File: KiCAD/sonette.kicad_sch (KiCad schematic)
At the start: 50 parts, among them J2 SERIAL_CON, J3 wav_selector, J4 Conn_01x08_Socket, J5 stlink, Q1 2N3904, Q2 2N3906, SW1 BELL, SW2 RESET, SW3 POWER, U1 W25Q80DV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

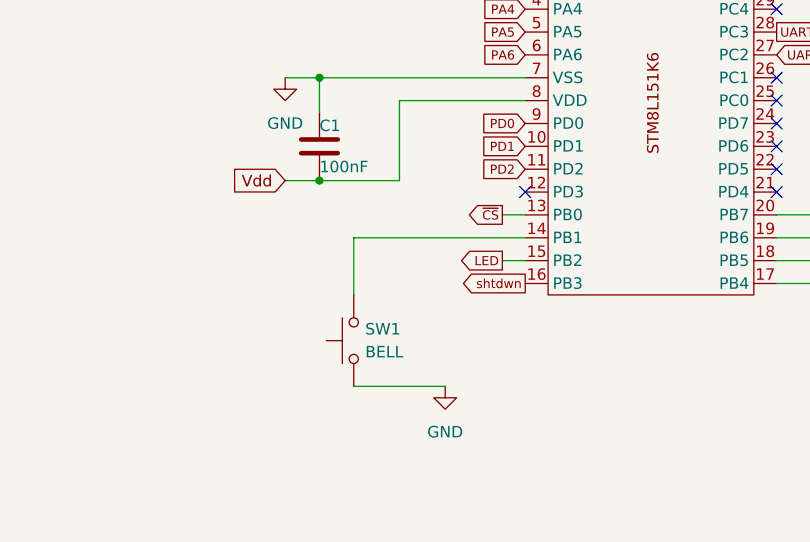
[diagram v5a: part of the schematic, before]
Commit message: Modification du circuit pour ajouter un circuit anti-interférance au bouton de la sonette. Ajout de R13 et C16.
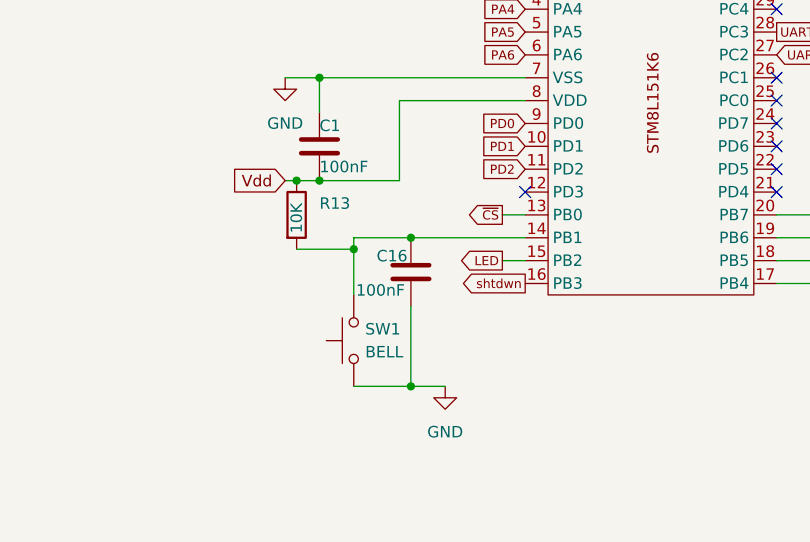
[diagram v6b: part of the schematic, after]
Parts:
- added C16: 100nF, symbol Device:C
- added R13: 10K, symbol Device:R
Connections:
- net GND: now also C16.2
- net Vdd: now also R13.1
- net at SW1.2, U2.14 (PB1): now also C16.1, R13.2
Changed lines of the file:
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@@
 	)
 	(junction
+		(at 76.2 148.59)
+		(diameter 0)
+		(color 0 0 0 0)
+	)
+	(junction
 		(at 66.04 130.81)
 		(diameter 0)
@@
 	)
 	(junction
+		(at 63.5 142.24)
+		(diameter 0)
+		(color 0 0 0 0)
+	)
+	(junction
 		(at 111.76 80.01)
 		(diameter 0)
@@
 	)
 	(junction
+		(at 76.2 165.1)
+		(diameter 0)
+		(color 0 0 0 0)
+	)
+	(junction
 		(at 86.36 36.83)
 		(diameter 0)
@@
 	)
 	(junction
+		(at 69.85 149.86)
+		(diameter 0)
+		(color 0 0 0 0)
+	)
+	(junction
 		(at 133.35 36.83)
 		(diameter 0)
@@
 	(wire
 		(pts
+			(xy 69.85 149.86) (xy 69.85 154.94)
+		)
+		(stroke
+			(width 0)
+			(type default)
+		)
+	)
+	(wire
+		(pts
 			(xy 210.82 82.55) (xy 203.2 82.55)
 		)
@@
 	(wire
 		(pts
+			(xy 76.2 156.21) (xy 76.2 165.1)
+		)
+		(stroke
+			(width 0)
+			(type default)
+		)
+	)
+	(wire
+		(pts
 			(xy 74.93 133.35) (xy 74.93 142.24)
 		)
@@
 	(wire
 		(pts
+			(xy 76.2 148.59) (xy 69.85 148.59)
+		)
+		(stroke
+			(width 0)
+			(type default)
+		)
+	)
+	(wire
+		(pts
 			(xy 124.46 41.91) (xy 125.73 41.91)
 		)
@@
 	(wire
 		(pts
-			(xy 62.23 142.24) (xy 66.04 142.24)
+			(xy 62.23 142.24) (xy 63.5 142.24)
 		)
 		(stroke
@@
 	(wire
 		(pts
-			(xy 69.85 148.59) (xy 69.85 154.94)
+			(xy 69.85 148.59) (xy 69.85 149.86)
 		)
 		(stroke
@@
 	(wire
 		(pts
-			(xy 69.85 165.1) (xy 80.01 165.1)
+			(xy 69.85 165.1) (xy 76.2 165.1)
 		)
 		(stroke
@@
 	(wire
 		(pts
-			(xy 88.9 148.59) (xy 69.85 148.59)
+			(xy 88.9 148.59) (xy 76.2 148.59)
 		)
 		(stroke
@@
 	(wire
 		(pts
+			(xy 63.5 142.24) (xy 66.04 142.24)
+		)
+		(stroke
+			(width 0)
+			(type default)
+		)
+	)
+	(wire
+		(pts
 			(xy 111.76 77.47) (xy 111.76 80.01)
 		)
@@
 	(wire
 		(pts
+			(xy 76.2 165.1) (xy 80.01 165.1)
+		)
+		(stroke
+			(width 0)
+			(type default)
+		)
+	)
+	(wire
+		(pts
 			(xy 111.76 74.93) (xy 111.76 77.47)
 		)
@@
 	(wire
 		(pts
+			(xy 63.5 149.86) (xy 69.85 149.86)
+		)
+		(stroke
+			(width 0)
+			(type default)
+		)
+	)
+	(wire
+		(pts
 			(xy 252.73 139.7) (xy 247.65 139.7)
 		)
@@
 	)
 	(symbol
+		(lib_id "Device:R")
+		(at 63.5 146.05 0)
+		(unit 1)
+		(exclude_from_sim no)
+		(in_bom yes)
+		(on_board yes)
+		(dnp no)
+		(property "Reference" "R13"
+			(at 66.04 144.7799 0)
+			(effects
+				(font
+					(size 1.27 1.27)
+				)
+				(justify left)
+			)
+		)
+		(property "Value" "10K"
+			(at 63.5 148.082 90)
+			(effects
+				(font
+					(size 1.27 1.27)
+				)
+				(justify left)
+			)
+		)
+		(property "Footprint" ""
+			(at 61.722 146.05 90)
+			(effects
+				(font
+					(size 1.27 1.27)
+				)
+				(hide yes)
+			)
+		)
+		(property "Datasheet" "~"
+			(at 63.5 146.05 0)
+			(effects
+				(font
+					(size 1.27 1.27)
+				)
+				(hide yes)
+			)
+		)
+		(property "Description" "Resistor"
+			(at 63.5 146.05 0)
+			(effects
+				(font
+					(size 1.27 1.27)
+				)
+				(hide yes)
+			)
+		)
+		(pin "2"
+		)
+		(pin "1"
+		)
+		(instances
+			(project ""
+				(path "/f9fee92e-b526-4b75-96ae-352cd94e2ffe"
+					(reference "R13")
+					(unit 1)
+				)
+			)
+		)
+	)
+	(symbol
 		(lib_id "Connector:Conn_01x08_Socket")
 		(at 96.52 72.39 0)
@@
 					(unit 1)
 				)
+			)
+		)
+	)
+	(symbol
+		(lib_id "Device:C")
+		(at 76.2 152.4 0)
+		(unit 1)
+		(exclude_from_sim no)
+		(in_bom yes)
+		(on_board yes)
+		(dnp no)
+		(property "Reference" "C16"
+			(at 72.39 150.622 0)
+			(effects
+				(font
+					(size 1.27 1.27)
+				)
+				(justify left)
+			)
+		)
+		(property "Value" "100nF"
+			(at 70.104 154.432 0)
+			(effects
+				(font
+					(size 1.27 1.27)
+				)
+				(justify left)
+			)
+		)
+		(property "Footprint" ""
+			(at 77.1652 156.21 0)
+			(effects
+				(font
+					(size 1.27 1.27)
+				)
+				(hide yes)
+			)
+		)
+		(property "Datasheet" "~"
+			(at 76.2 152.4 0)
+			(effects
+				(font
+					(size 1.27 1.27)
+				)
+				(hide yes)
+			)
+		)
+		(property "Description" "Unpolarized capacitor"
+			(at 76.2 152.4 0)
+			(effects
+				(font
+					(size 1.27 1.27)
+				)
+				(hide yes)
+			)
+		)
+		(pin "2"
+		)
+		(pin "1"
+		)
+		(instances
+			(project "sonette"
+				(path "/f9fee92e-b526-4b75-96ae-352cd94e2ffe"
+					(reference "C16")
+					(unit 1)
+				)

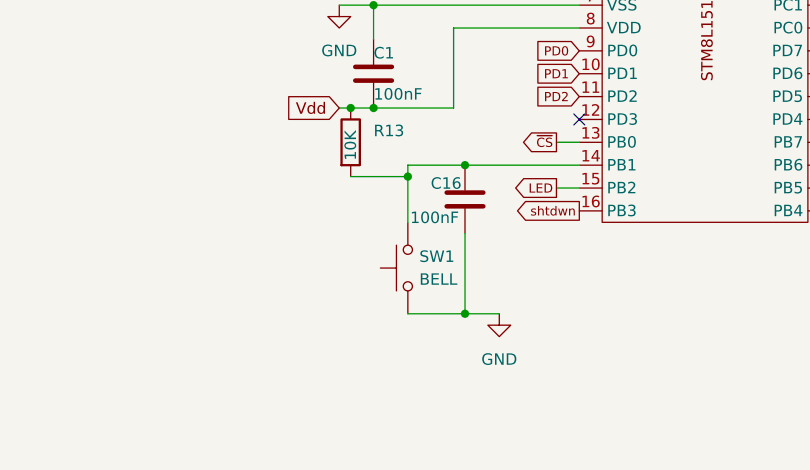
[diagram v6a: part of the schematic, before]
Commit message: Modification du circuit pour ajouter la résistance de 1Ko en série avec le fil du bouton de la sonnette. Le fil agissant comme une antenne captait les impulsion RF ce qui avait pour effet de déclencher la sonnerie.
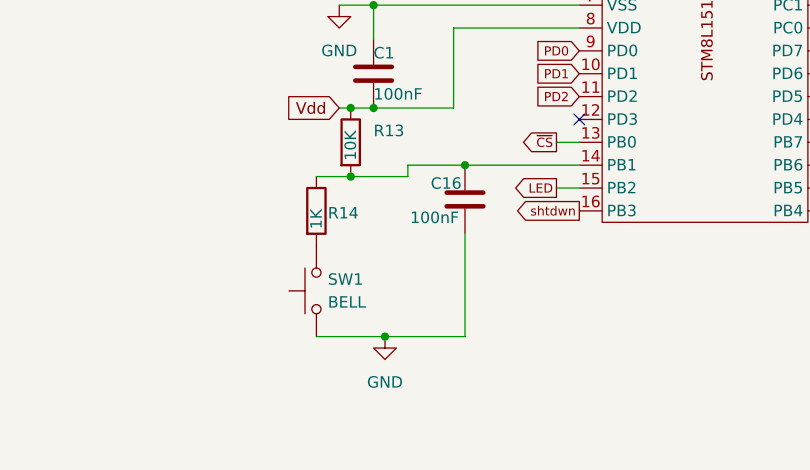
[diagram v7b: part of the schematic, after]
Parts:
- added R14: 1K, symbol Device:R
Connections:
- net at C16.1, R13.2, U2.14 (PB1): now also R14.1; no longer SW1.2
- new net: R14.2, SW1.2
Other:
- moved on the sheet: SW1
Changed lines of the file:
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@@
 	)
 	(junction
-		(at 72.39 49.53)
+		(at 67.31 167.64)
 		(diameter 0)
 		(color 0 0 0 0)
 	)
 	(junction
-		(at 148.59 138.43)
+		(at 63.5 149.86)
 		(diameter 0)
 		(color 0 0 0 0)
 	)
 	(junction
-		(at 184.15 96.52)
+		(at 72.39 49.53)
 		(diameter 0)
 		(color 0 0 0 0)
 	)
 	(junction
-		(at 158.75 118.11)
+		(at 148.59 138.43)
 		(diameter 0)
 		(color 0 0 0 0)
 	)
 	(junction
-		(at 111.76 82.55)
+		(at 184.15 96.52)
 		(diameter 0)
 		(color 0 0 0 0)
 	)
 	(junction
-		(at 241.3 142.24)
+		(at 158.75 118.11)
 		(diameter 0)
 		(color 0 0 0 0)
 	)
 	(junction
-		(at 76.2 165.1)
+		(at 111.76 82.55)
 		(diameter 0)
 		(color 0 0 0 0)
 	)
 	(junction
-		(at 86.36 36.83)
+		(at 241.3 142.24)
 		(diameter 0)
 		(color 0 0 0 0)
 	)
 	(junction
-		(at 69.85 149.86)
+		(at 86.36 36.83)
 		(diameter 0)
 		(color 0 0 0 0)
@@
 	(wire
 		(pts
-			(xy 69.85 149.86) (xy 69.85 154.94)
-		)
-		(stroke
-			(width 0)
-			(type default)
-		)
-	)
-	(wire
-		(pts
 			(xy 210.82 82.55) (xy 203.2 82.55)
 		)
@@
 	(wire
 		(pts
-			(xy 76.2 156.21) (xy 76.2 165.1)
-		)
-		(stroke
-			(width 0)
-			(type default)
-		)
-	)
-	(wire
-		(pts
 			(xy 74.93 133.35) (xy 74.93 142.24)
 		)
@@
 	(wire
 		(pts
-			(xy 69.85 165.1) (xy 76.2 165.1)
+			(xy 59.69 167.64) (xy 67.31 167.64)
 		)
 		(stroke
@@
 	(wire
 		(pts
+			(xy 76.2 156.21) (xy 76.2 167.64)
+		)
+		(stroke
+			(width 0)
+			(type default)
+		)
+	)
+	(wire
+		(pts
 			(xy 87.63 64.77) (xy 91.44 64.77)
 		)
@@
 	(wire
 		(pts
+			(xy 67.31 167.64) (xy 76.2 167.64)
+		)
+		(stroke
+			(width 0)
+			(type default)
+		)
+	)
+	(wire
+		(pts
+			(xy 59.69 149.86) (xy 63.5 149.86)
+		)
+		(stroke
+			(width 0)
+			(type default)
+		)
+	)
+	(wire
+		(pts
 			(xy 143.51 125.73) (xy 148.59 125.73)
 		)
@@
 	(wire
 		(pts
-			(xy 76.2 165.1) (xy 80.01 165.1)
-		)
-		(stroke
-			(width 0)
-			(type default)
-		)
-	)
-	(wire
-		(pts
 			(xy 111.76 74.93) (xy 111.76 77.47)
 		)
@@
 	(symbol
 		(lib_id "Switch:SW_Push")
-		(at 69.85 160.02 90)
+		(at 59.69 162.56 90)
 		(unit 1)
 		(exclude_from_sim no)
@@
 		(fields_autoplaced yes)
 		(property "Reference" "SW1"
-			(at 71.12 158.7499 90)
+			(at 60.96 161.2899 90)
 			(effects
 				(font
@@
 		)
 		(property "Value" "BELL"
-			(at 71.12 161.2899 90)
+			(at 60.96 163.8299 90)
 			(effects
 				(font
@@
 		)
 		(property "Footprint" ""
-			(at 64.77 160.02 0)
+			(at 54.61 162.56 0)
 			(effects
 				(font
@@
 		)
 		(property "Datasheet" "~"
-			(at 64.77 160.02 0)
+			(at 54.61 162.56 0)
 			(effects
 				(font
@@
 		)
 		(property "Description" "Push button switch, generic, two pins"
-			(at 69.85 160.02 0)
+			(at 59.69 162.56 0)
 			(effects
 				(font
@@
 	(symbol
 		(lib_id "power:GND")
-		(at 80.01 165.1 0)
+		(at 67.31 167.64 0)
 		(unit 1)
 		(exclude_from_sim no)
@@
 		(fields_autoplaced yes)
 		(property "Reference" "#PWR04"
-			(at 80.01 171.45 0)
+			(at 67.31 173.99 0)
 			(effects
 				(font
@@
 		)
 		(property "Value" "GND"
-			(at 80.01 170.18 0)
+			(at 67.31 172.72 0)
 			(effects
 				(font
@@
 		)
 		(property "Footprint" ""
-			(at 80.01 165.1 0)
+			(at 67.31 167.64 0)
 			(effects
 				(font
@@
 		)
 		(property "Datasheet" ""
-			(at 80.01 165.1 0)
+			(at 67.31 167.64 0)
 			(effects
 				(font
@@
 		)
 		(property "Description" "Power symbol creates a global label with name \"GND\" , ground"
-			(at 80.01 165.1 0)
+			(at 67.31 167.64 0)
 			(effects
 				(font
@@
 					(unit 1)
 				)
+			)
+		)
+	)
+	(symbol
+		(lib_id "Device:R")
+		(at 59.69 153.67 0)
+		(unit 1)
+		(exclude_from_sim no)
+		(in_bom yes)
+		(on_board yes)
+		(dnp no)
+		(property "Reference" "R14"
+			(at 60.96 153.924 0)
+			(effects
+				(font
+					(size 1.27 1.27)
+				)
+				(justify left)
+			)
+		)
+		(property "Value" "1K"
+			(at 59.69 155.702 90)
+			(effects
+				(font
+					(size 1.27 1.27)
+				)
+				(justify left)
+			)
+		)
+		(property "Footprint" ""
+			(at 57.912 153.67 90)
+			(effects
+				(font
+					(size 1.27 1.27)
+				)
+				(hide yes)
+			)
+		)
+		(property "Datasheet" "~"
+			(at 59.69 153.67 0)
+			(effects
+				(font
+					(size 1.27 1.27)
+				)
+				(hide yes)
+			)
+		)
+		(property "Description" "Resistor"
+			(at 59.69 153.67 0)
+			(effects
+				(font
+					(size 1.27 1.27)
+				)
+				(hide yes)
+			)
+		)
+		(pin "2"
+		)
+		(pin "1"
+		)
+		(instances
+			(project "sonette"
+				(path "/f9fee92e-b526-4b75-96ae-352cd94e2ffe"
+					(reference "R14")
+					(unit 1)
+				)
